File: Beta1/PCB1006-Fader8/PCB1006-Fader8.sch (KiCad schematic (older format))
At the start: 32 parts, among them J1 USB-K, U1000 MCP3008T-I/SL

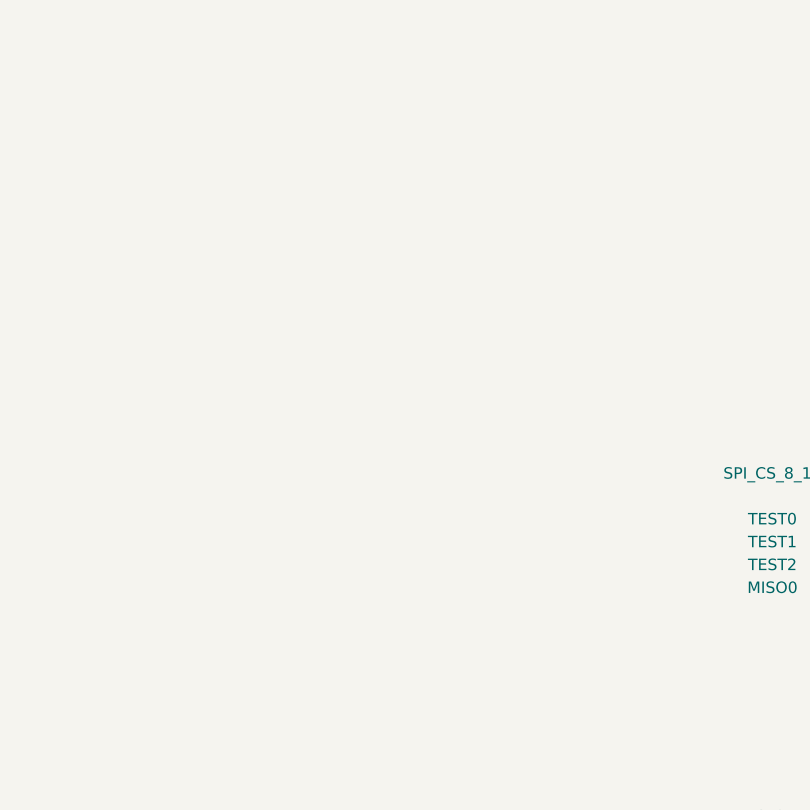
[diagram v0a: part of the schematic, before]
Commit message: Conversion to FFC WIP
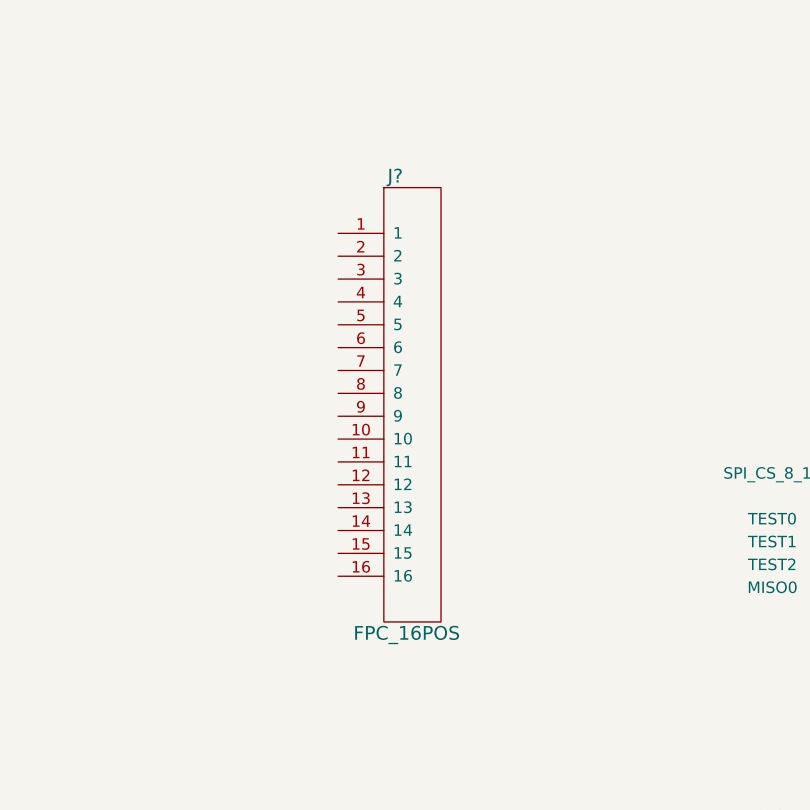
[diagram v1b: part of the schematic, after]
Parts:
- added J?: FPC_16POS, symbol FPC_16POS
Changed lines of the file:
@@
+	1    0    0    -1
+$EndComp
+$Comp
+L FPC_16POS J?
+U 1 1 596EA02E
+P 6050 3350
+F 0 "J?" H 6100 3600 60  0000 C CNN
+F 1 "FPC_16POS" H 6150 1600 60  0000 C CNN
+F 2 "" H 5850 2900 60  0001 C CNN
+F 3 "" H 5850 2900 60  0001 C CNN
+	1    6050 3350
 	1    0    0    -1
 $EndComp

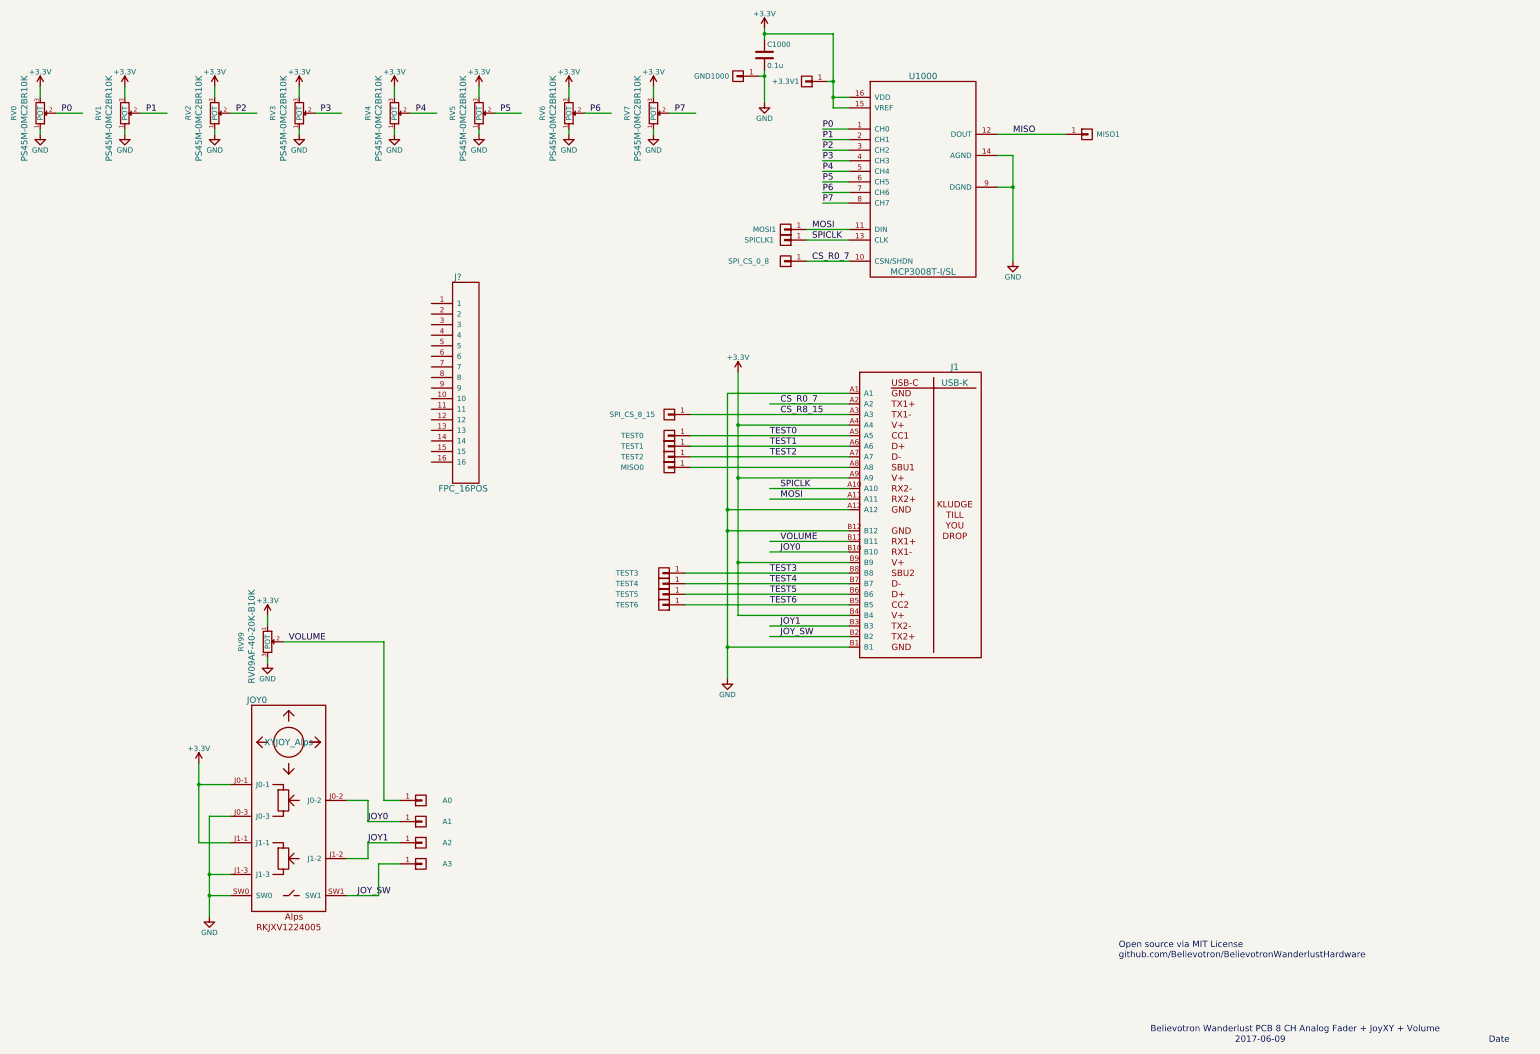
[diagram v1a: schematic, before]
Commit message: Swapped USBK for FFC connector. Routed.
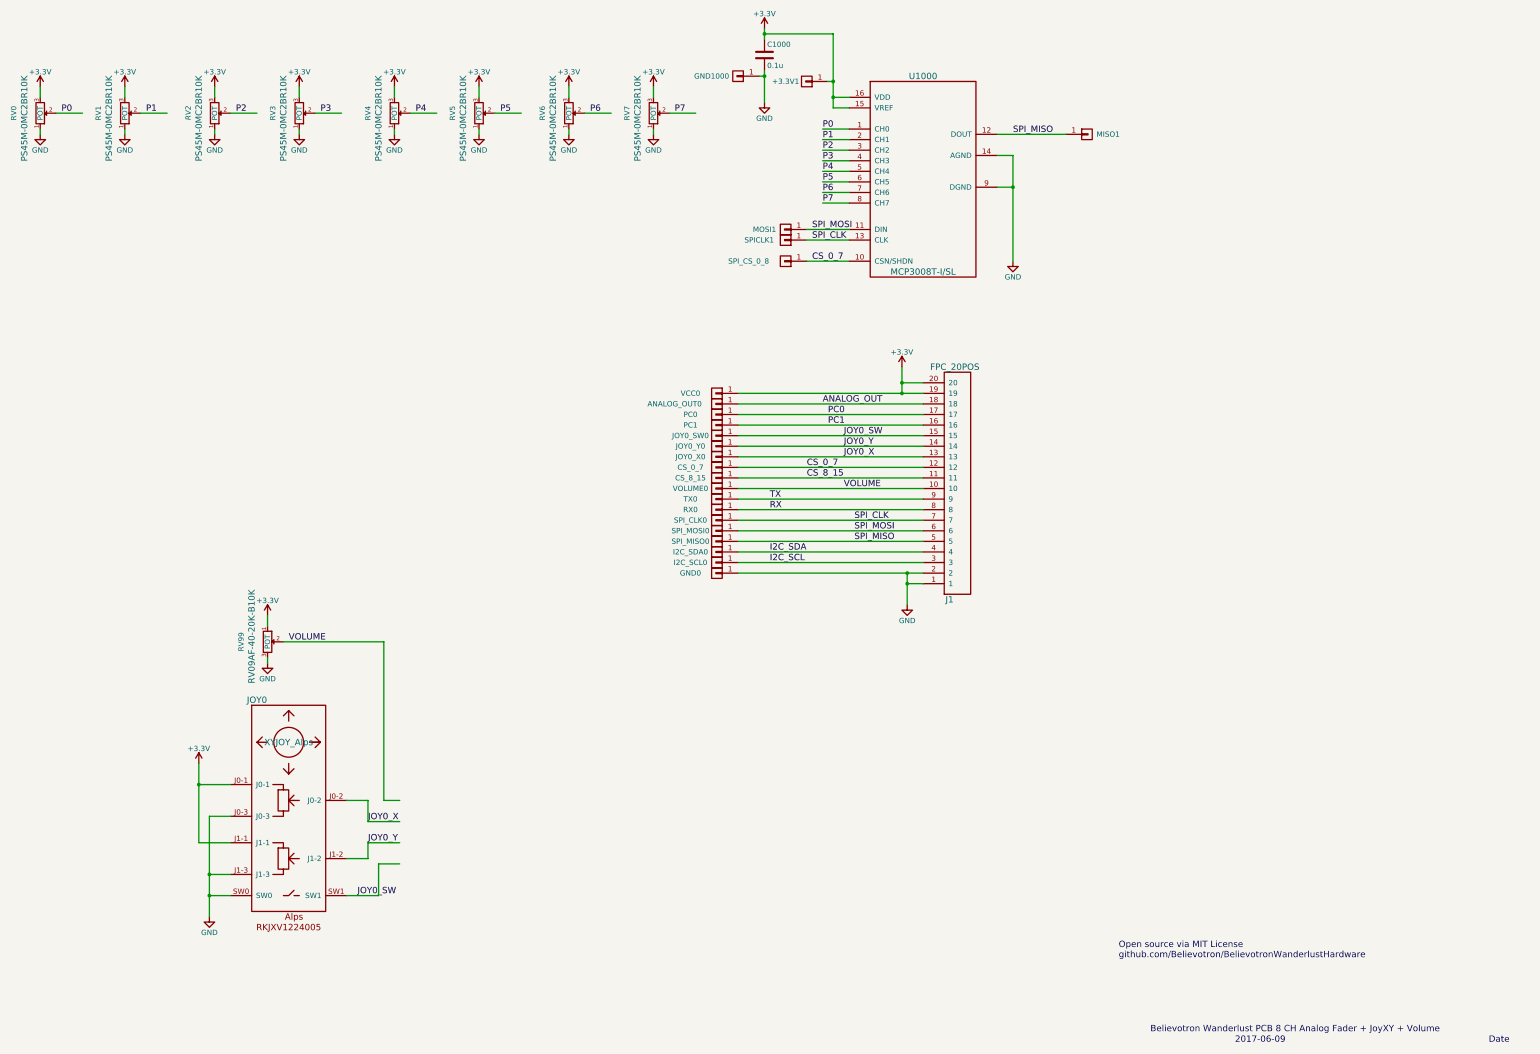
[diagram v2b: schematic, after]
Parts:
- removed A0, A1, A2, A3: CONN_01X01, Liberry:single_0.1, symbol CONN_01X01
- removed J1: USB-K, Liberry:USB-K_12401610E4_2A, symbol USB-K
- removed J?: FPC_16POS, symbol FPC_16POS
- removed MISO0, SPI_CS_8_15, TEST0, TEST1, TEST2, TEST3, TEST4, TEST5, TEST6: CONN_01X01, Liberry:TH_0.1_1x2_Jumper, symbol CONN_01X01
- added ANALOG_OUT0, CS_0_7, CS_8_15, GND0, I2C_SCL0, I2C_SDA0, JOY0_SW0, JOY0_X0, JOY0_Y0, PC0, PC1, RX0, SPI_CLK0, SPI_MISO0, SPI_MOSI0, TX0, VCC0, VOLUME0: CONN_01X01, Liberry:TH_0.1_1x2_Jumper, symbol CONN_01X01
- added J1: FPC_20POS, Liberry:FFC_1MM_20POS_MOLEX_52271-2079, symbol FPC_20POS
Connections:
- net labels added: ANALOG_OUT, CS_0_7, CS_8_15, I2C_SCL, I2C_SDA, JOY0_SW, JOY0_X, JOY0_Y, PC0, PC1, RX, SPI_CLK, SPI_MISO, SPI_MOSI, TX
- net labels removed: CS_R0_7, CS_R8_15, JOY0, JOY1, JOY_SW, MISO, MOSI, SPICLK, TEST0, TEST1, TEST2, TEST3, TEST4, TEST5, TEST6
- wire segments 94 -> 90
